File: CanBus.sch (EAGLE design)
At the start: 47 parts, among them IC1 MCP2515-I/SO, IC2 MEGA8-P, IC3 MCP2515-I/SO, Q1 16MHz, Q2 16MHz, Q3 16MHz, U1 MCP2562-E/SN, U2 MCP2562-E/SN, X1 MAC64L

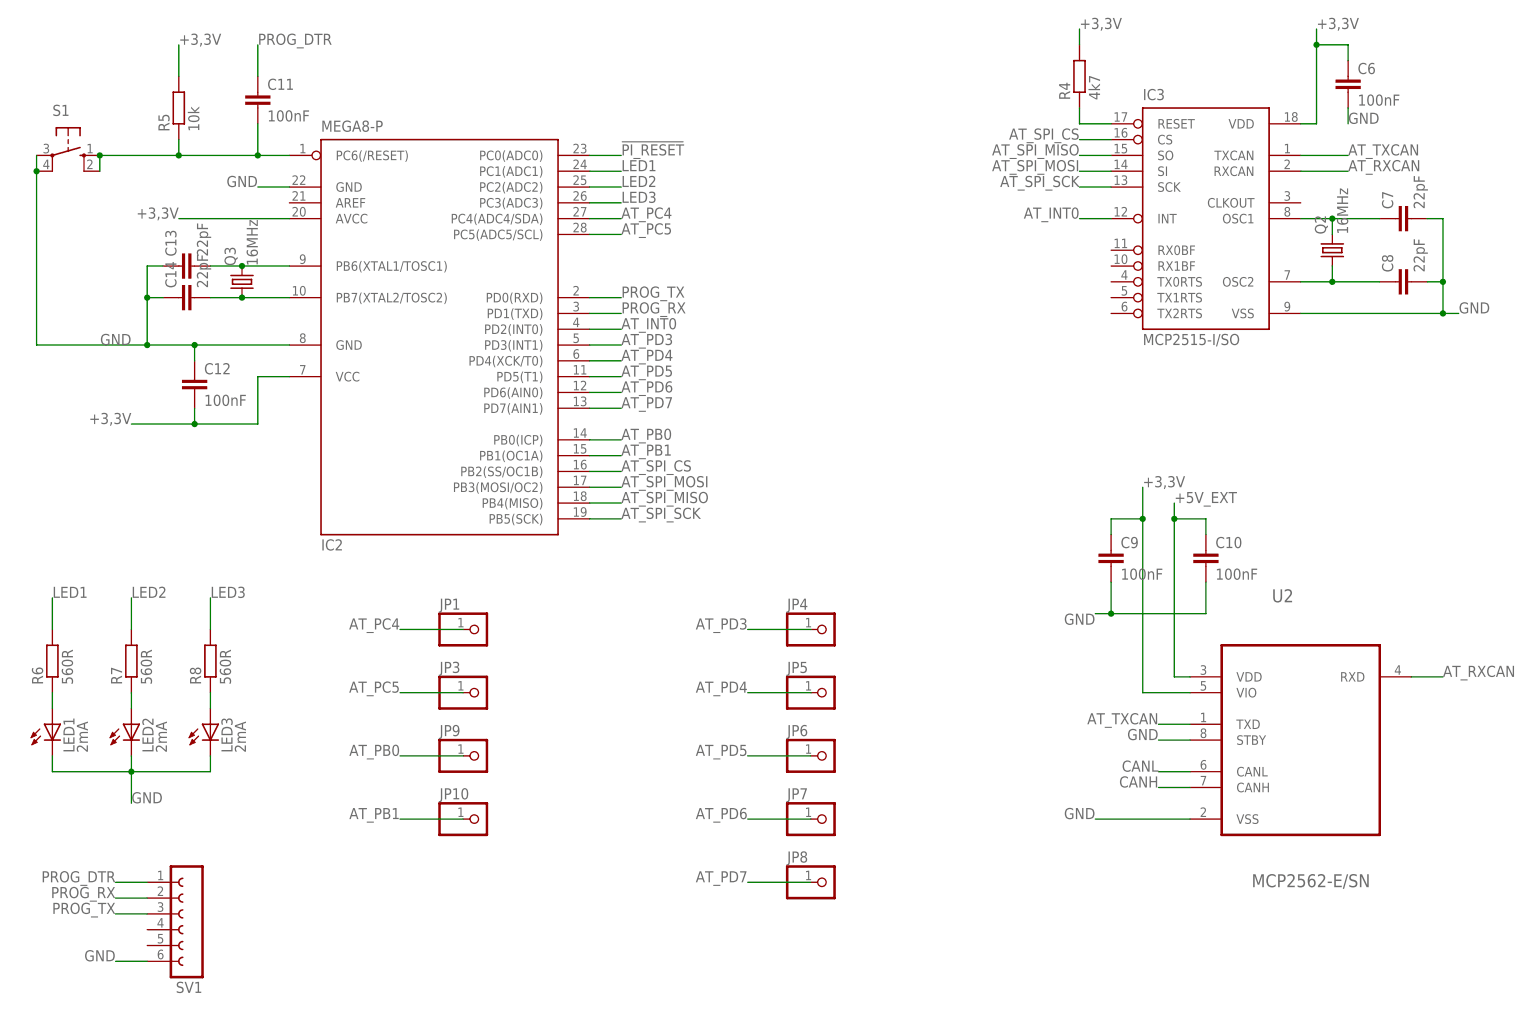
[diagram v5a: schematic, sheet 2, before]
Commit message: Layouts aktualisiert, Neue Libs
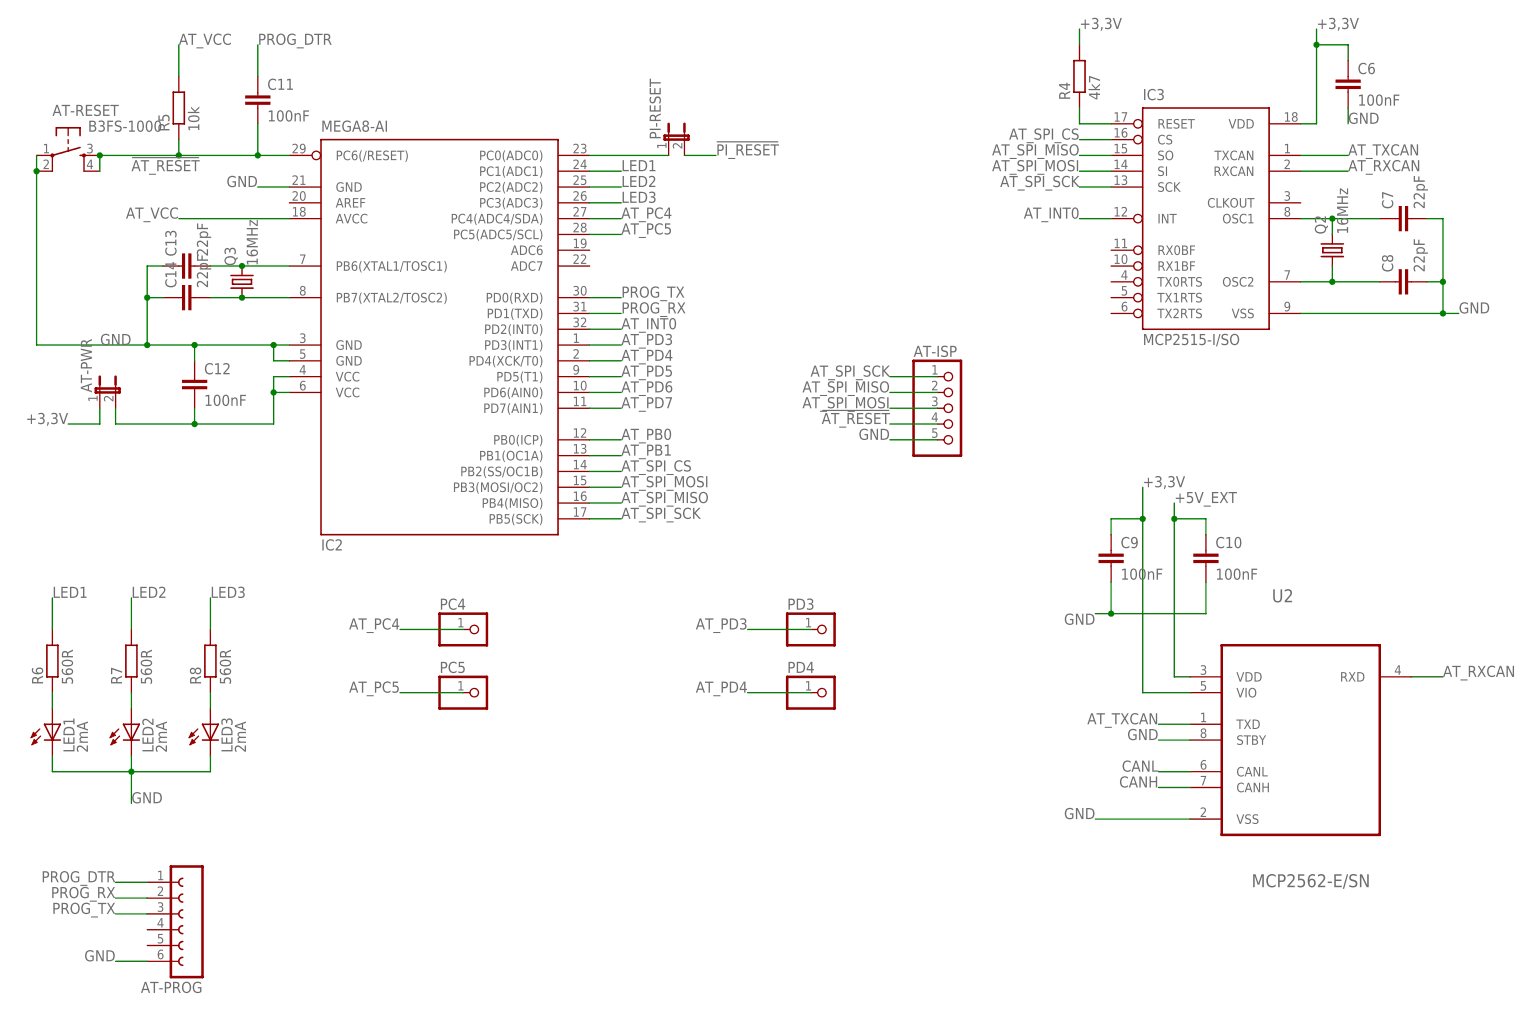
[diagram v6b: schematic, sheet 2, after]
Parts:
- removed JP10, JP6, JP7, JP8, JP9: (no value), pinhead:PINHD-1X1
- removed S1: (no value), switch-omron:10-XX
- added AT-ISP: (no value), pinhead:PINHD-1X5
- added AT-PWR, PI-RESET: (no value), jumper:JP1E
- added AT-RESET: B3FS-1000, b3fs-1000:B3FS-1000
- IC2: value MEGA8-P -> MEGA8-AI; device atmel:MEGA8-P -> atmel:MEGA8-AI
- renumbered JP1 to PC4, JP3 to PC5, JP4 to PD3, JP5 to PD4, SV1 to AT-PROG
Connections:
- removed net N$8: C11.2, IC2.PC6(/RESET), R5.1, S1.S, S1.S1
- new net !AT_RESET: AT-ISP.4, AT-RESET.S, AT-RESET.S1, C11.2, IC2.PC6(/RESET), R5.1
- new net AT_VCC: AT-PWR.2, C12.2, IC2.AVCC, IC2.VCC@1, IC2.VCC@2, R5.2
- new net N$9: IC2.PC0(ADC0), PI-RESET.1
- net !PI_RESET: now also PI-RESET.2; no longer IC2.PC0(ADC0)
- net +3,3V: now also AT-PWR.1; no longer C12.2, IC2.AVCC, IC2.VCC@1, R5.2
- net AT_PB0: no longer JP9.1
- net AT_PB1: no longer JP10.1
- net AT_PD5: no longer JP6.1
- net AT_PD6: no longer JP7.1
- net AT_PD7: no longer JP8.1
- net AT_SPI_MISO: now also AT-ISP.2
- net AT_SPI_MOSI: now also AT-ISP.3
- net AT_SPI_SCK: now also AT-ISP.1
- net GND: now also AT-RESET.P, AT-RESET.P1, IC2.GND@2; no longer S1.P, S1.P1

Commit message: Layouts angepasst
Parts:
- added A14, A15, A16, A17, A18, A19, A20, A21, A22, PB0, PB1, PD5, PD6, PD7: (no value), pinhead:PINHD-1X1
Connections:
- new net A14: A14.1, X1.A14
- new net A15: A15.1, X1.A15
- new net A16: A16.1, X1.A16
- new net A17: A17.1, X1.A17
- new net A18: A18.1, X1.A18
- new net A19: A19.1, X1.A19
- new net A20: A20.1, X1.A20
- new net A21: A21.1, X1.A21
- new net A22: A22.1, X1.A22
- new net A23: X1.A23
- new net A24: X1.A24
- new net A25: X1.A25
- new net N$12: X1.A4
- new net N$16: X1.A7
- new net N$8: X1.A5
- net !AT_RESET: now also AT-ISP.5; no longer AT-ISP.4
- net 1WIRE: now also X1.C7; no longer X1.A7
- net AT_PB0: now also PB0.1
- net AT_PB1: now also PB1.1
- net AT_PD5: now also PD5.1
- net AT_PD6: now also PD6.1
- net AT_PD7: now also PD7.1
- net AT_SPI_MISO: now also AT-ISP.3; no longer AT-ISP.2
- net AT_SPI_MOSI: now also AT-ISP.4; no longer AT-ISP.3
- net AT_SPI_SCK: now also AT-ISP.2; no longer AT-ISP.1
- net GND: now also AT-ISP.1, X1.A11, X1.A13, X1.A27, X1.C13
- net I2C_SCL: now also X1.C5; no longer X1.A5
- net I2C_SDA: now also X1.C4; no longer X1.A4
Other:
- moved on the sheet: AT-ISP, J1, PC4, PC5

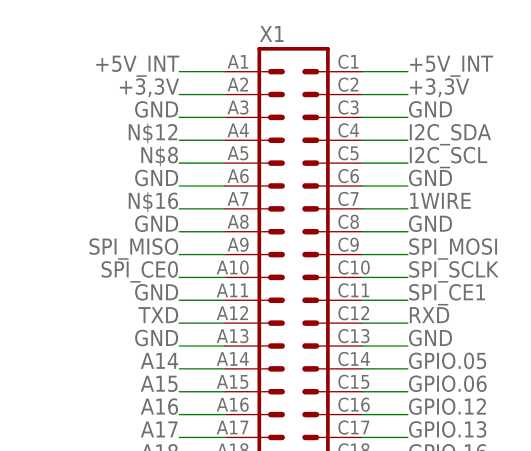
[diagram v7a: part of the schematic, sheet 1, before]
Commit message: CAN-Bus Beadboard-Adapter, Layouts angepasst
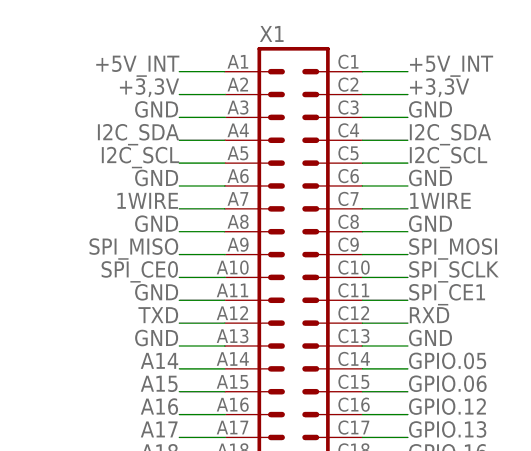
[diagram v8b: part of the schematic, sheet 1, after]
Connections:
- removed net N$12: X1.A4
- removed net N$16: X1.A7
- removed net N$8: X1.A5
- net 1WIRE: now also X1.A7
- net I2C_SCL: now also X1.A5
- net I2C_SDA: now also X1.A4
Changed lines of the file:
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@@
 <grid distance="0.1" unitdist="inch" unit="inch" style="lines" multiple="1" display="no" altdistance="0.01" altunitdist="inch" altunit="inch"/>
 <layers>
-<layer number="1" name="Top" color="4" fill="1" visible="yes" active="no"/>
-<layer number="2" name="Route2" color="1" fill="3" visible="yes" active="no"/>
-<layer number="3" name="Route3" color="4" fill="3" visible="yes" active="no"/>
-<layer number="4" name="Route4" color="1" fill="4" visible="yes" active="no"/>
-<layer number="5" name="Route5" color="4" fill="4" visible="yes" active="no"/>
-<layer number="6" name="Route6" color="1" fill="8" visible="yes" active="no"/>
-<layer number="7" name="Route7" color="4" fill="8" visible="yes" active="no"/>
-<layer number="8" name="Route8" color="1" fill="2" visible="yes" active="no"/>
-<layer number="9" name="Route9" color="4" fill="2" visible="yes" active="no"/>
-<layer number="10" name="Route10" color="1" fill="7" visible="yes" active="no"/>
-<layer number="11" name="Route11" color="4" fill="7" visible="yes" active="no"/>
-<layer number="12" name="Route12" color="1" fill="5" visible="yes" active="no"/>
-<layer number="13" name="Route13" color="4" fill="5" visible="yes" active="no"/>
-<layer number="14" name="Route14" color="1" fill="6" visible="yes" active="no"/>
-<layer number="15" name="Route15" color="4" fill="6" visible="yes" active="no"/>
-<layer number="16" name="Bottom" color="1" fill="1" visible="yes" active="no"/>
-<layer number="17" name="Pads" color="2" fill="1" visible="yes" active="no"/>
-<layer number="18" name="Vias" color="2" fill="1" visible="yes" active="no"/>
-<layer number="19" name="Unrouted" color="6" fill="1" visible="yes" active="no"/>
-<layer number="20" name="Dimension" color="15" fill="1" visible="yes" active="no"/>
-<layer number="21" name="tPlace" color="7" fill="1" visible="yes" active="no"/>
-<layer number="22" name="bPlace" color="7" fill="1" visible="yes" active="no"/>
-<layer number="23" name="tOrigins" color="15" fill="1" visible="yes" active="no"/>
-<layer number="24" name="bOrigins" color="15" fill="1" visible="yes" active="no"/>
-<layer number="25" name="tNames" color="7" fill="1" visible="yes" active="no"/>
-<layer number="26" name="bNames" color="7" fill="1" visible="yes" active="no"/>
-<layer number="27" name="tValues" color="7" fill="1" visible="yes" active="no"/>
-<layer number="28" name="bValues" color="7" fill="1" visible="yes" active="no"/>
+<layer number="1" name="Top" color="4" fill="1" visible="no" active="no"/>
+<layer number="2" name="Route2" color="1" fill="3" visible="no" active="no"/>
+<layer number="3" name="Route3" color="4" fill="3" visible="no" active="no"/>
+<layer number="4" name="Route4" color="1" fill="4" visible="no" active="no"/>
+<layer number="5" name="Route5" color="4" fill="4" visible="no" active="no"/>
+<layer number="6" name="Route6" color="1" fill="8" visible="no" active="no"/>
+<layer number="7" name="Route7" color="4" fill="8" visible="no" active="no"/>
+<layer number="8" name="Route8" color="1" fill="2" visible="no" active="no"/>
+<layer number="9" name="Route9" color="4" fill="2" visible="no" active="no"/>
+<layer number="10" name="Route10" color="1" fill="7" visible="no" active="no"/>
+<layer number="11" name="Route11" color="4" fill="7" visible="no" active="no"/>
+<layer number="12" name="Route12" color="1" fill="5" visible="no" active="no"/>
+<layer number="13" name="Route13" color="4" fill="5" visible="no" active="no"/>
+<layer number="14" name="Route14" color="1" fill="6" visible="no" active="no"/>
+<layer number="15" name="Route15" color="4" fill="6" visible="no" active="no"/>
+<layer number="16" name="Bottom" color="1" fill="1" visible="no" active="no"/>
+<layer number="17" name="Pads" color="2" fill="1" visible="no" active="no"/>
+<layer number="18" name="Vias" color="2" fill="1" visible="no" active="no"/>
+<layer number="19" name="Unrouted" color="6" fill="1" visible="no" active="no"/>
+<layer number="20" name="Dimension" color="15" fill="1" visible="no" active="no"/>
+<layer number="21" name="tPlace" color="7" fill="1" visible="no" active="no"/>
+<layer number="22" name="bPlace" color="7" fill="1" visible="no" active="no"/>
+<layer number="23" name="tOrigins" color="15" fill="1" visible="no" active="no"/>
+<layer number="24" name="bOrigins" color="15" fill="1" visible="no" active="no"/>
+<layer number="25" name="tNames" color="7" fill="1" visible="no" active="no"/>
+<layer number="26" name="bNames" color="7" fill="1" visible="no" active="no"/>
+<layer number="27" name="tValues" color="7" fill="1" visible="no" active="no"/>
+<layer number="28" name="bValues" color="7" fill="1" visible="no" active="no"/>
 <layer number="29" name="tStop" color="7" fill="3" visible="no" active="no"/>
 <layer number="30" name="bStop" color="7" fill="6" visible="no" active="no"/>
@@
 <layer number="35" name="tGlue" color="7" fill="4" visible="no" active="no"/>
 <layer number="36" name="bGlue" color="7" fill="5" visible="no" active="no"/>
-<layer number="37" name="tTest" color="7" fill="1" visible="yes" active="no"/>
-<layer number="38" name="bTest" color="7" fill="1" visible="yes" active="no"/>
+<layer number="37" name="tTest" color="7" fill="1" visible="no" active="no"/>
+<layer number="38" name="bTest" color="7" fill="1" visible="no" active="no"/>
 <layer number="39" name="tKeepout" color="4" fill="11" visible="no" active="no"/>
 <layer number="40" name="bKeepout" color="1" fill="11" visible="no" active="no"/>
@@
 <layer number="44" name="Drills" color="7" fill="1" visible="no" active="no"/>
 <layer number="45" name="Holes" color="7" fill="1" visible="no" active="no"/>
-<layer number="46" name="Milling" color="3" fill="1" visible="yes" active="no"/>
-<layer number="47" name="Measures" color="7" fill="1" visible="yes" active="no"/>
-<layer number="48" name="Document" color="7" fill="1" visible="yes" active="no"/>
-<layer number="49" name="Reference" color="7" fill="1" visible="yes" active="no"/>
-<layer number="50" name="dxf" color="7" fill="1" visible="yes" active="no"/>
-<layer number="51" name="tDocu" color="7" fill="1" visible="yes" active="no"/>
-<layer number="52" name="bDocu" color="7" fill="1" visible="yes" active="no"/>
-<layer number="53" name="tGND_GNDA" color="7" fill="1" visible="yes" active="no"/>
-<layer number="54" name="bGND_GNDA" color="7" fill="1" visible="yes" active="no"/>
-<layer number="56" name="wert" color="7" fill="1" visible="yes" active="no"/>
+<layer number="46" name="Milling" color="3" fill="1" visible="no" active="no"/>
+<layer number="47" name="Measures" color="7" fill="1" visible="no" active="no"/>
+<layer number="48" name="Document" color="7" fill="1" visible="no" active="no"/>
+<layer number="49" name="Reference" color="7" fill="1" visible="no" active="no"/>
+<layer number="50" name="dxf" color="7" fill="1" visible="no" active="no"/>
+<layer number="51" name="tDocu" color="7" fill="1" visible="no" active="no"/>
+<layer number="52" name="bDocu" color="7" fill="1" visible="no" active="no"/>
+<layer number="53" name="tGND_GNDA" color="7" fill="1" visible="no" active="no"/>
+<layer number="54" name="bGND_GNDA" color="7" fill="1" visible="no" active="no"/>
+<layer number="56" name="wert" color="7" fill="1" visible="no" active="no"/>
 <layer number="90" name="Modules" color="5" fill="1" visible="yes" active="yes"/>
 <layer number="91" name="Nets" color="2" fill="1" visible="yes" active="yes"/>
@@
 <label x="60.96" y="152.4" size="1.778" layer="95"/>
 </segment>
+<segment>
+<pinref part="X1" gate="G$1" pin="A4"/>
+<wire x1="40.64" y1="152.4" x2="35.56" y2="152.4" width="0.1524" layer="91"/>
+<label x="35.56" y="152.4" size="1.778" layer="95" rot="MR0"/>
+</segment>
 </net>
 <net name="I2C_SCL" class="0">
@@
 <label x="60.96" y="149.86" size="1.778" layer="95"/>
 </segment>
+<segment>
+<pinref part="X1" gate="G$1" pin="A5"/>
+<wire x1="40.64" y1="149.86" x2="35.56" y2="149.86" width="0.1524" layer="91"/>
+<label x="35.56" y="149.86" size="1.778" layer="95" rot="MR0"/>
+</segment>
 </net>
 <net name="1WIRE" class="0">
@@
 <wire x1="55.88" y1="144.78" x2="60.96" y2="144.78" width="0.1524" layer="91"/>
 <label x="60.96" y="144.78" size="1.778" layer="95"/>
+</segment>
+<segment>
+<pinref part="X1" gate="G$1" pin="A7"/>
+<wire x1="40.64" y1="144.78" x2="35.56" y2="144.78" width="0.1524" layer="91"/>
+<label x="35.56" y="144.78" size="1.778" layer="95" rot="MR0"/>
 </segment>
 </net>
@@
 <wire x1="40.64" y1="96.52" x2="35.56" y2="96.52" width="0.1524" layer="91"/>
 <label x="35.56" y="96.52" size="1.778" layer="95" rot="MR0"/>
-</segment>
-</net>
-<net name="N$8" class="0">
-<segment>
-<pinref part="X1" gate="G$1" pin="A5"/>
-<wire x1="40.64" y1="149.86" x2="35.56" y2="149.86" width="0.1524" layer="91"/>
-<label x="35.56" y="149.86" size="1.778" layer="95" rot="MR0"/>
-</segment>
-</net>
-<net name="N$12" class="0">
-<segment>
-<pinref part="X1" gate="G$1" pin="A4"/>
-<wire x1="40.64" y1="152.4" x2="35.56" y2="152.4" width="0.1524" layer="91"/>
-<label x="35.56" y="152.4" size="1.778" layer="95" rot="MR0"/>
-</segment>
-</net>
-<net name="N$16" class="0">
-<segment>
-<pinref part="X1" gate="G$1" pin="A7"/>
-<wire x1="40.64" y1="144.78" x2="35.56" y2="144.78" width="0.1524" layer="91"/>
-<label x="35.56" y="144.78" size="1.778" layer="95" rot="MR0"/>
 </segment>
 </net>
@@
 <junction x="35.56" y="96.52"/>
 <pinref part="AT-PWR" gate="A" pin="2"/>
+<label x="22.86" y="96.52" size="1.778" layer="95"/>
 </segment>
 <segment>
@@
 </sheet>
 </sheets>
+<errors>
+</errors>
 </schematic>
 </drawing>
